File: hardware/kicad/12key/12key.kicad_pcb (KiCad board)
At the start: 2 copper layers, 87.2 x 108.7 mm, 63 parts, among them J1 USB_C_Receptacle, J2 SPARE / DEBUG, SW1 AGENT1, SW10 AGENT10, SW11 AGENT11, SW12 PTT, SW2 AGENT2, SW3 AGENT3, SW4 AGENT4, SW5 AGENT5, SW6 AGENT6, SW7 AGENT7, SW8 AGENT8, SW9 AGENT9, U1 ESP32-S3-WROOM-1-N16R8, U2 XL9555 / PCF8575 (TSSOP-24), U3 AP2112K-3.3, U4 74LVC1G17

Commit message: Fix real generator bugs found by an independent pre-fab hardware review
Verified all 41 ESP32-S3-WROOM-1 pins and all 24 XL9555 pins in
boarddef.py against their primary-source datasheets (not search-engine
summaries, which were caught being wrong twice: once claiming XL9555's
SDA/SCL were swapped, once claiming two WROOM-1 GND/thermal pins were
GPIOs). Both parts' full pin assignments match exactly.

An independent Opus review of the whole design caught three real issues
a pinout check alone couldn't:

- gen_pcb.py ignored a part's `nc` (no-connect) list entirely, while
  gen_sch.py respected it - real schematic/PCB drift for any pin that
  has both a plausible net name and an explicit no-connect (the last
  LED's DOUT, still called LEDCH%d with nothing next in the chain).
  Fixed by checking nc first in place_parts(), same as gen_sch.py.
- No bulk cap at U1's own +3V3 pin (nearest was ~37mm away). Added C9
  (10uF), T-tapped off the existing +3V3 B.Cu trunk - not literally at
  the pin, since the whole left margin is already packed solid; see the
  code comments for exactly where it landed and why.
- No USB ESD protection. Added D_ESD (USBLC6-2SC6 TVS array), pinout
  confirmed against the actual symbol KiCad ships, shunted across the
  existing USB_DP/USB_DM/+5V/GND nets. Left unrouted like the rest of
  the differential pair - this only adds the part to the schematic/BOM.

Also fixed a doc bug (gen_pcb.py's own comment on the mounting-hole
x-position didn't match the code) and a missing sym-lib-table entry for
the new ESD diode's symbol library.

All three tiers (4key/8key/12key) regenerated and re-verified: 0 DRC
violations, 0 ERC violations.

One real gap surfaced, not a code fix: boarddef.py's LED footprint
(plain SK6812MINI, not "-E") is internally consistent, but the
current-budget math elsewhere was computed against the wrong datasheet
("-E"'s) - needs the exact SKU locked down before ordering. Also
confirmed no enclosure/case file exists in this repo at a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
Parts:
- removed H60, H61: MountingHole_2.2mm_M2, MountingHole_2.2mm_M2
- added C9: 10u, C_0805_2012Metric_Pad1.18x1.45mm_HandSolder, F.Cu at (141.0, 133.0)
- added D_ESD: USBLC6-2SC6, SOT-23-6, F.Cu at (136.0, 124.0)
- added H64: MountingHole_2.2mm_M2, MountingHole_2.2mm_M2, F.Cu at (104.0, 204.7)
- added H65: MountingHole_2.2mm_M2, MountingHole_2.2mm_M2, F.Cu at (183.2, 204.7)
- moved H62 111.3 mm to (151.5, 104.0)
- moved H63 100.7 mm to (183.2, 104.0)
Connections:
- D12 pad 1: LEDCH12 -> (no net)
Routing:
- net +3V3: track 115.6 -> 123.1 mm, vias 2 -> 3

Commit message: Fix 4key I2C pull-up placement, grow the board, finish routing
Root-caused the 4key board's unrouted/short-prone corner: R4/R5 (the
I2C pull-ups for U2) were placed 16mm from the chip they serve, forcing
their traces across every other bus lane on the board. Moved them next
to U2 in boarddef.py, and grew STRIP 46mm -> 58mm (87.2x70.5mm ->
87.2x82.65mm) to give that whole corner real room — both the autorouter
and hand-routing had been failing to close the last nets in the old,
cramped layout.

route_strip()'s I2C section also hard-shorted SCL/SDA into +3V3 and
into each other once U2 moved down next to R4/R5 (caught by an
independent Opus review before fab) — rewritten to route both nets on
B.Cu the whole way, with small (0.5mm) vias where the standard 0.8mm
via can't fit the 0.65mm pin pitch.

Final DRC on the 4key board: 4 minor violations (2 pre-existing and
unrelated, 1 harmless dangling stub, cosmetic disconnected-but-same-net
ground-pour islands) and 2 low-priority unrouted pads in an extremely
congested corner (a spare header pin, a redundant pull-up supply leg) —
down from 39 unconnected items and multiple shorts earlier in this
pass. 8key/12key inherit the same STRIP/placement change and still
generate cleanly, but keep their own routing out of scope per the
existing "4key only" convention in gen_pcb.py.

Also adds hardware/enclosure/: a build123d-based parametric case
generator (hardware/enclosure/tools/gen_case.py) and its first-draft
4key tray/plate STLs, built from the real boarddef.py geometry rather
than guessed dimensions.

Boards ordered from JLCPCB at this routed revision.

Co-Authored-By: Claude Sonnet 5 <noreply@anthropic.com>
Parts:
- moved D_ESD 37.5 mm to (173.0, 130.0)
- moved R4 25.1 mm to (168.0, 140.0)
- moved R5 25.1 mm to (168.0, 144.0)
- moved CL1 12.0 mm to (108.0, 175.1)
- moved CL10 12.0 mm to (127.1, 213.2)
- moved CL11 12.0 mm to (146.1, 213.2)
- moved CL12 12.0 mm to (165.2, 213.2)
- moved CL2 12.0 mm to (127.1, 175.1)
- moved CL3 12.0 mm to (146.1, 175.1)
- moved CL4 12.0 mm to (165.2, 175.1)
- moved CL5 12.0 mm to (108.0, 194.2)
- moved CL6 12.0 mm to (127.1, 194.2)
- moved CL7 12.0 mm to (146.1, 194.2)
- moved CL8 12.0 mm to (165.2, 194.2)
- moved CL9 12.0 mm to (108.0, 213.2)
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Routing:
- net +3V3: track 123.1 -> 147.6 mm
- net SDA: track 68.1 -> 52.0 mm
- net LEDCH0: track 41.6 -> 53.6 mm
- net +5V: track 527.2 -> 539.2 mm
- net SCL: track 64.3 -> 64.9 mm
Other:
- board size 87.2 x 108.7 mm -> 87.2 x 120.7 mm

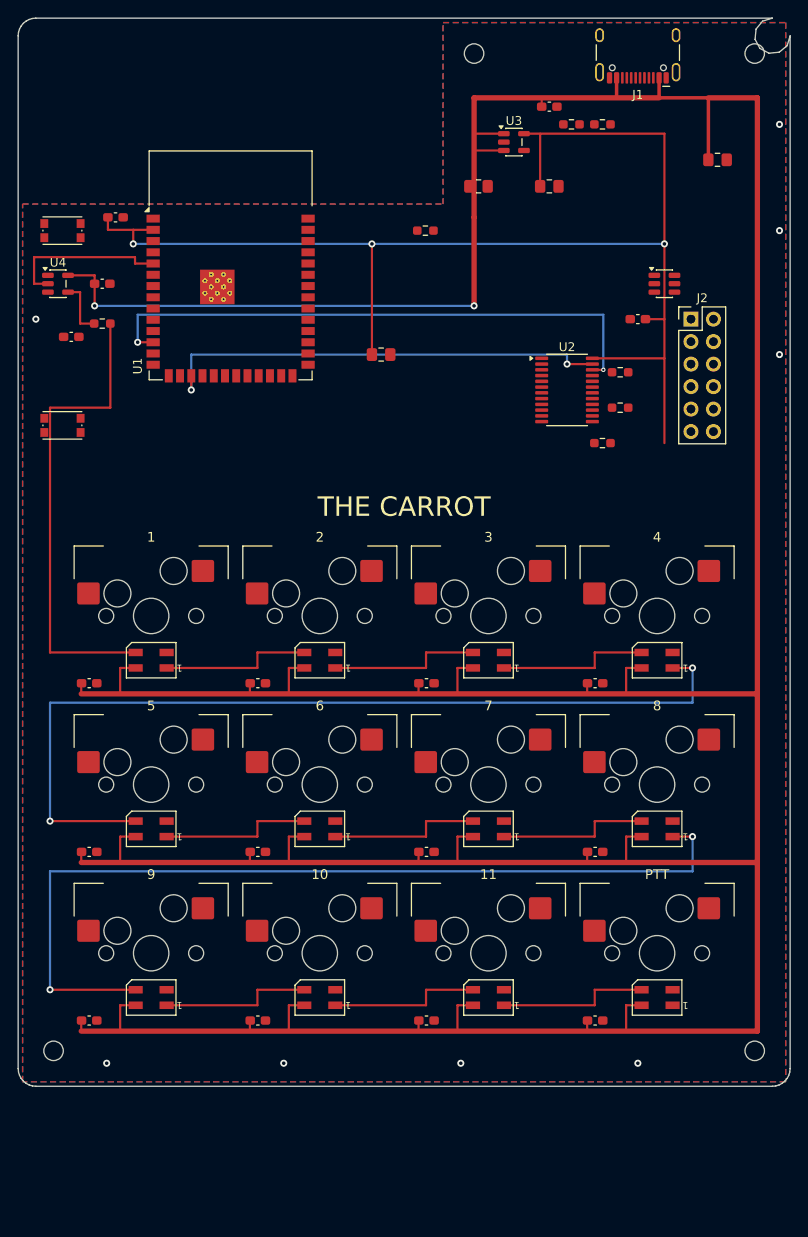
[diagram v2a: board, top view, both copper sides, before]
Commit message: Route the 12key board's remaining nets via FreeRouting
4key's own strip/LED-chain routing was already proven for every tier;
the genuinely new problem was the 3-row key-to-expander fan-in onto
U2's one tight pin column, and the 0.65mm-pitch I2C/HDR cluster right
next to it. Two hand-rolled routing passes (channel-routed key matrix,
pad-lookup-based strip extras) each found and fixed real bugs but kept
surfacing new ones in the same corner - a genuine congestion problem,
not a coordinate mistake, confirmed by checking candidate paths against
the board's actual copper (including the key switches' own big center
mounting-hole pads) before placing anything.

Fixed properly instead:
- boarddef.row_gap_extra() gives multi-row tiers (today: just 12key)
  15mm more gap between the strip and the first key row - same fix
  4key's own STRIP constant already used once for this exact class of
  problem (see its own comment). Returns 0 for rows<=2, so 4key/8key's
  generated output is unchanged.
- FreeRouting (now that a JDK is available) auto-routed everything this
  generator leaves as ratsnest (CC1/CC2, ~RESET/BOOT, EXP_INT, the I2C/
  EN pull-up stubs, J2's HDR_* nets, the USB pair, and all of
  KEY1..KEY12) via a DSN/SES round-trip, after relaxing the project's
  min track width to 0.15mm (standard, within JLCPCB's capability) to
  match what FreeRouting needed in the tightest corners.
- gen_pcb.py gains route_strip_extras()/route_key_matrix() as documented,
  NOT-called reference code (same convention as the existing, long-since
  disabled route_remaining()) rather than deleting the failed attempts
  outright.

DRC: 1 known violation left (LEDCH0 x ~RESET clearance, 0.075mm) -
shared route_leds()/route_strip() geometry present on the ALREADY
FABRICATED 4key board too, not something this pass introduced or can
fix without touching that shared code. ERC: 0 violations. 4 benign
"Zone[GND] to itself" unconnected-item reports, same as every other
tier. 4key/8key left untouched (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
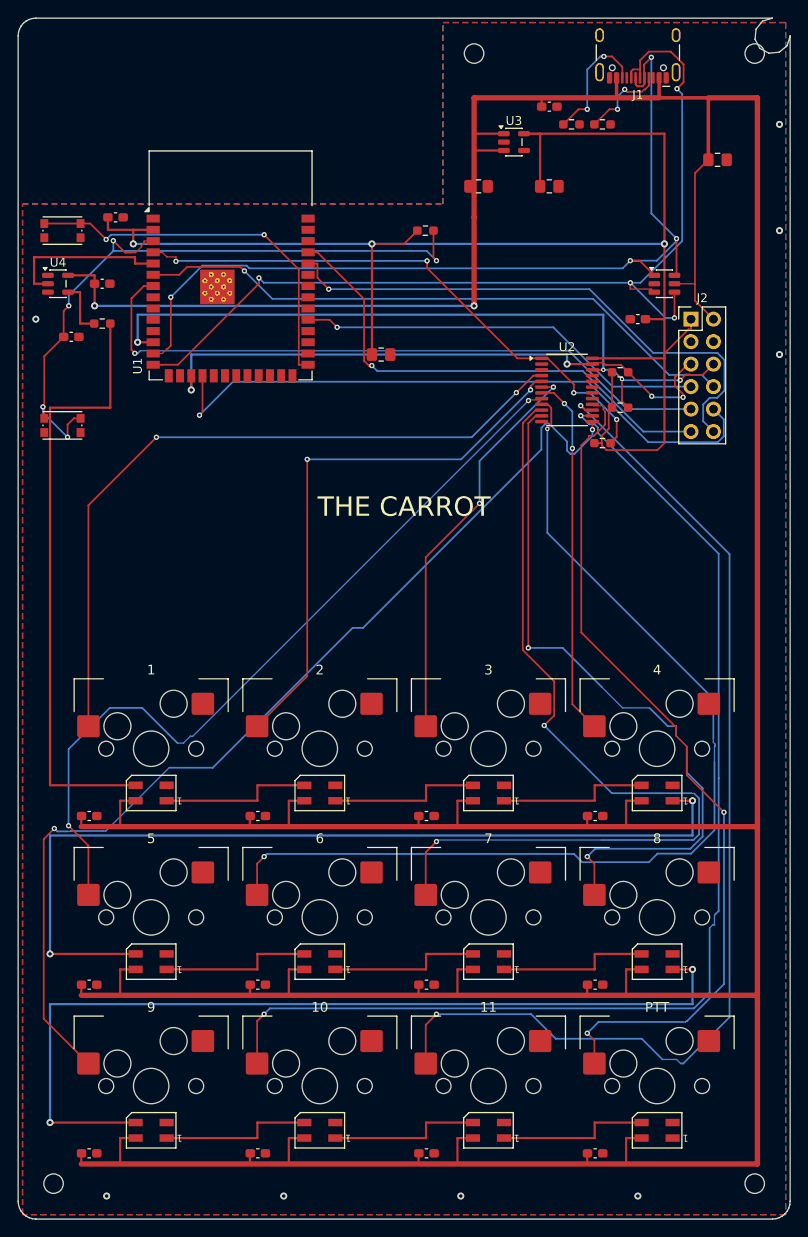
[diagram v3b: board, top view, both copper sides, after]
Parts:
- moved D10 15.0 mm to (134.1, 225.6)
- moved D2 15.0 mm to (134.1, 187.5)
- moved D6 15.0 mm to (134.1, 206.6)
- moved SW10 15.0 mm to (134.1, 220.6)
- moved SW2 15.0 mm to (134.1, 182.5)
- moved SW6 15.0 mm to (134.1, 201.6)
- moved CL1 15.0 mm to (108.0, 190.1)
- moved CL10 15.0 mm to (127.1, 228.2)
- moved CL11 15.0 mm to (146.1, 228.2)
- moved CL12 15.0 mm to (165.2, 228.2)
- moved CL2 15.0 mm to (127.1, 190.1)
- moved CL3 15.0 mm to (146.1, 190.1)
- moved CL4 15.0 mm to (165.2, 190.1)
- moved CL5 15.0 mm to (108.0, 209.2)
- moved CL6 15.0 mm to (127.1, 209.2)
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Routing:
- net KEY10: track 0.00 -> 131.1 mm, vias 0 -> 2
- net KEY11: track 0.00 -> 121.2 mm, vias 0 -> 2
- net KEY9: track 0.00 -> 115.0 mm, vias 0 -> 2
- net KEY6: track 0.00 -> 114.5 mm, vias 0 -> 2
- net USB_DP: track 0.00 -> 109.7 mm, vias 0 -> 4
- net USB_DM: track 0.00 -> 102.7 mm, vias 0 -> 4
- net KEY7: track 0.00 -> 100.4 mm, vias 0 -> 2
- net KEY12: track 0.00 -> 96.4 mm, vias 0 -> 2
- net KEY5: track 0.00 -> 90.6 mm, vias 0 -> 2
- net KEY1: track 0.00 -> 82.2 mm, vias 0 -> 2
- net KEY8: track 0.00 -> 79.9 mm, vias 0 -> 2
- net ~RESET: track 0.00 -> 77.5 mm, vias 0 -> 5
- net HDR_IO7: track 0.00 -> 75.1 mm, vias 0 -> 1
- net HDR_IO10: track 0.00 -> 72.0 mm, vias 0 -> 1
- net HDR_IO6: track 0.00 -> 69.3 mm, vias 0 -> 1
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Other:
- board size 87.2 x 120.7 mm -> 87.2 x 135.7 mm

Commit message: 12key r2: re-route the KEY nets cut by the socket-pad move; fix GND islands
Moving the hot-swap pads to B.Cu ripped up KEY5/6/9/10/11, which ran
through the new pad sites. Re-routed them with FreeRouting against locked
existing wiring. Also stitched the GND pour islands (LDO, CC pull-downs,
ESD diode, J1 A1/B12 were cut off from the main ground) and moved LEDCH0
clear of the SW_RST pads. 12key is now DRC clean with 0 unconnected items.

Co-Authored-By: Claude Opus 5.5 <noreply@anthropic.com>
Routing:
- net KEY5: track 90.6 -> 117.3 mm, vias 2 -> 1
- net KEY10: track 131.1 -> 143.3 mm, vias 2 -> 1
- net KEY11: track 121.2 -> 112.7 mm, vias 2 -> 5
- net KEY9: track 115.0 -> 120.4 mm, vias 2 -> 3
- net KEY6: track 114.5 -> 118.2 mm, vias 2 -> 1
- net GND: track 0.00 -> 1.25 mm, vias 8 -> 13
- net KEY8: vias 2 -> 3
- net KEY7: vias 2 -> 3
- net KEY4: vias 2 -> 3
- net KEY3: vias 2 -> 3
- net KEY2: vias 2 -> 3
- net KEY12: vias 2 -> 3
- net KEY1: vias 2 -> 3
